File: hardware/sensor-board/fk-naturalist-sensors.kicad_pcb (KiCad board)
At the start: 2 copper layers, 20 x 32 mm, 18 parts, among them J1 Conn_01x07, M1 MOUNT_HOLE, M2 MOUNT_HOLE, M3 MOUNT_HOLE, M4 MOUNT_HOLE, U1 MPL3115A2, U2 SHT31, U3 SPH0645, U4 TSL2591

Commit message: Adding fiducials to the sensor board.
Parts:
- added M5: FIDUCIAL, Fiducials:Fiducial_0.75mm_Dia_1.5mm_Outer, F.Cu at (230.3, 129.8)
- added M6: FIDUCIAL, Fiducials:Fiducial_0.75mm_Dia_1.5mm_Outer, F.Cu at (237.9, 113.1)
- added M7: FIDUCIAL, Fiducials:Fiducial_0.75mm_Dia_1.5mm_Outer, F.Cu at (222.0, 109.9)
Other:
- board text added: "v0.9"
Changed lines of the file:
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@@
-(kicad_pcb (version 4) (host pcbnew 4.0.7-e2-6376~58~ubuntu16.04.1)
+(kicad_pcb (version 4) (host pcbnew 4.0.7)
   (general
     (links 39)
-    (no_connects 0)
+    (no_connects 14)
     (area 219.924999 99.924999 240.075001 132.075001)
     (thickness 1.6)
-    (drawings 4)
+    (drawings 5)
     (tracks 123)
     (zones 0)
-    (modules 18)
-    (nets 16)
+    (modules 21)
+    (nets 19)
   )
   (page A4)
@@
   (net 14 "Net-(U4-Pad2)")
   (net 15 "Net-(U4-Pad4)")
+  (net 16 "Net-(M5-Pad~)")
+  (net 17 "Net-(M6-Pad~)")
+  (net 18 "Net-(M7-Pad~)")
   (net_class Default "This is the default net class."
     (clearance 0.2)
@@
     (add_net GND)
     (add_net "Net-(C1-Pad1)")
+    (add_net "Net-(M5-Pad~)")
+    (add_net "Net-(M6-Pad~)")
+    (add_net "Net-(M7-Pad~)")
     (add_net "Net-(R1-Pad2)")
     (add_net "Net-(R2-Pad1)")
@@
     )
   )
+  (module Fiducials:Fiducial_0.75mm_Dia_1.5mm_Outer (layer F.Cu)
+    (at 230.251 129.794)
+    (descr "Circular Fiducial, 0.75mm bare copper top; 1.5mm keepout (Level B)")
+    (tags marker)
+    (attr virtual)
+    (fp_text reference M5 (at 0 -2) (layer F.SilkS) hide
+      (effects (font (size 1 1) (thickness 0.15)))
+    )
+    (fp_text value FIDUCIAL (at 0 2) (layer F.Fab) hide
+      (effects (font (size 1 1) (thickness 0.15)))
+    )
+    (fp_circle (center 0 0) (end 0.75 0) (layer F.Fab) (width 0.1))
+    (fp_text user %R (at 0 0) (layer F.Fab)
+      (effects (font (size 0.3 0.3) (thickness 0.05)))
+    )
+    (fp_circle (center 0 0) (end 1 0) (layer F.CrtYd) (width 0.05))
+    (pad ~ smd circle (at 0 0) (size 0.75 0.75) (layers F.Cu F.Mask)
+      (net 16 "Net-(M5-Pad~)") (solder_mask_margin 0.375) (clearance 0.375))
+  )
+  (module Fiducials:Fiducial_0.75mm_Dia_1.5mm_Outer (layer F.Cu)
+    (at 237.874 113.119001)
+    (descr "Circular Fiducial, 0.75mm bare copper top; 1.5mm keepout (Level B)")
+    (tags marker)
+    (attr virtual)
+    (fp_text reference M6 (at 0 -2) (layer F.SilkS) hide
+      (effects (font (size 1 1) (thickness 0.15)))
+    )
+    (fp_text value FIDUCIAL (at 0 2) (layer F.Fab) hide
+      (effects (font (size 1 1) (thickness 0.15)))
+    )
+    (fp_circle (center 0 0) (end 0.75 0) (layer F.Fab) (width 0.1))
+    (fp_text user %R (at 0 0) (layer F.Fab)
+      (effects (font (size 0.3 0.3) (thickness 0.05)))
+    )
+    (fp_circle (center 0 0) (end 1 0) (layer F.CrtYd) (width 0.05))
+    (pad ~ smd circle (at 0 0) (size 0.75 0.75) (layers F.Cu F.Mask)
+      (net 17 "Net-(M6-Pad~)") (solder_mask_margin 0.375) (clearance 0.375))
+  )
+  (module Fiducials:Fiducial_0.75mm_Dia_1.5mm_Outer (layer F.Cu)
+    (at 221.996 109.855)
+    (descr "Circular Fiducial, 0.75mm bare copper top; 1.5mm keepout (Level B)")
+    (tags marker)
+    (attr virtual)
+    (fp_text reference M7 (at 0 -2) (layer F.SilkS) hide
+      (effects (font (size 1 1) (thickness 0.15)))
+    )
+    (fp_text value FIDUCIAL (at 0 2) (layer F.Fab) hide
+      (effects (font (size 1 1) (thickness 0.15)))
+    )
+    (fp_circle (center 0 0) (end 0.75 0) (layer F.Fab) (width 0.1))
+    (fp_text user %R (at 0 0) (layer F.Fab)
+      (effects (font (size 0.3 0.3) (thickness 0.05)))
+    )
+    (fp_circle (center 0 0) (end 1 0) (layer F.CrtYd) (width 0.05))
+    (pad ~ smd circle (at 0 0) (size 0.75 0.75) (layers F.Cu F.Mask)
+      (net 18 "Net-(M7-Pad~)") (solder_mask_margin 0.375) (clearance 0.375))
+  )
+  (gr_text v0.9 (at 228.219 101.473 180) (layer F.SilkS)
+    (effects (font (size 1.5 1.5) (thickness 0.3)))
+  )
   (gr_line (start 240 100) (end 220 100) (layer Edge.Cuts) (width 0.15))

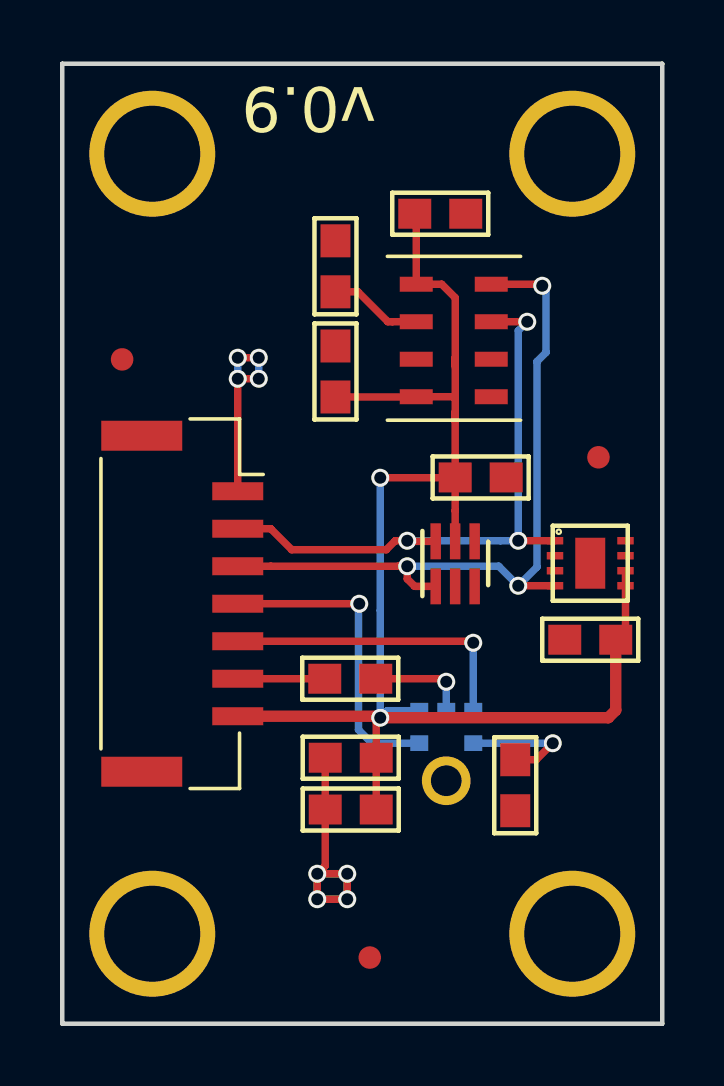
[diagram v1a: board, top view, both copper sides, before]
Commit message: Using new SPH0645 footprint.
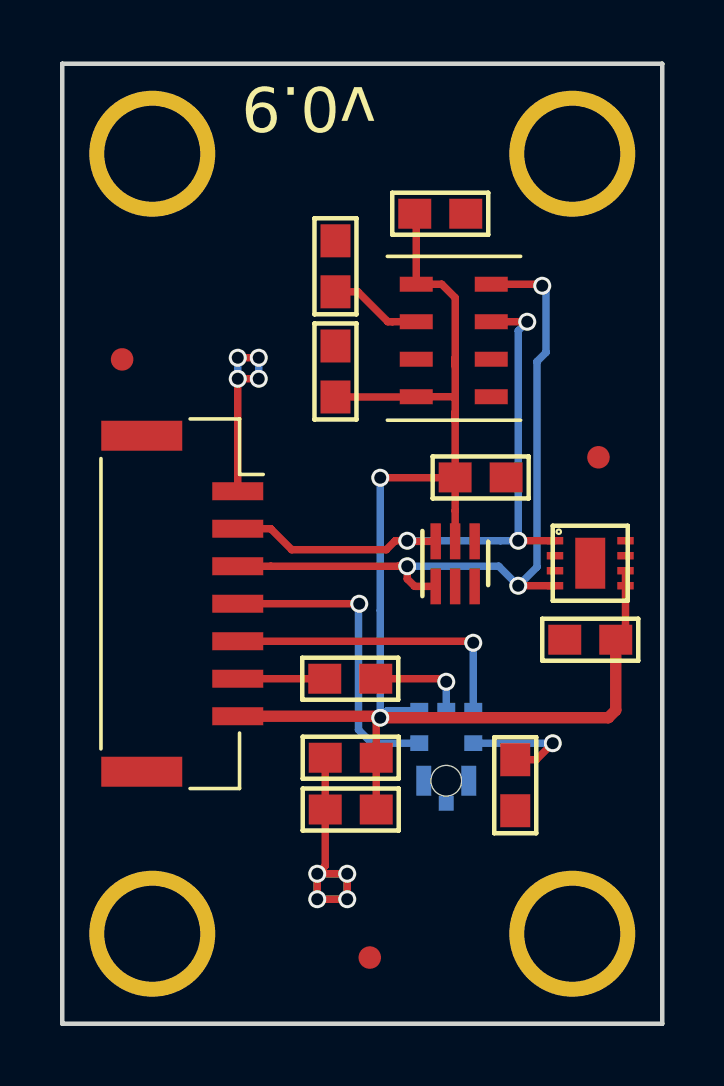
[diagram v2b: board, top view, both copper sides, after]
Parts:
- U3: footprint conservify:SPH0645LM4H-B -> SPH0645LM4H-B-SMD-GND
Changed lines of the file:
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@@
 (kicad_pcb (version 4) (host pcbnew 4.0.7)
   (general
-    (links 39)
-    (no_connects 14)
-    (area 219.924999 99.924999 240.075001 132.075001)
+    (links 41)
+    (no_connects 3)
+    (area 217.990476 98.85 242.009524 133.25)
     (thickness 1.6)
     (drawings 5)
@@
     (37 F.SilkS user)
     (38 B.Mask user)
-    (39 F.Mask user)
+    (39 F.Mask user hide)
     (40 Dwgs.User user)
     (41 Cmts.User user)
@@
     (add_net "Net-(U4-Pad4)")
   )
+  (module SPH0645LM4H-B-SMD-GND (layer B.Cu)
+    (at 232.8 123.9 180)
+    (fp_text reference U3 (at 0 3.302 180) (layer B.SilkS) hide
+      (effects (font (size 1 1) (thickness 0.15)) (justify mirror))
+    )
+    (fp_text value SPH0645 (at 0 -1.8 180) (layer B.Fab) hide
+      (effects (font (size 1 1) (thickness 0.15)) (justify mirror))
+    )
+    (fp_circle (center 0 0) (end 0.5 0) (layer Dwgs.User) (width 0.01))
+    (fp_circle (center 0 0) (end 0.8 0.05) (layer Dwgs.User) (width 0.01))
+    (fp_line (start -1.4 -1) (end 1.4 -1) (layer B.SilkS) (width 0.1))
+    (fp_line (start 1.4 -1) (end 1.4 2.7) (layer B.SilkS) (width 0.1))
+    (fp_line (start 1.4 2.7) (end -1.4 2.7) (layer B.SilkS) (width 0.1))
+    (fp_line (start -1.4 2.7) (end -1.4 -1) (layer B.SilkS) (width 0.1))
+    (pad 4 smd rect (at 0.9 1.252 180) (size 0.6 0.522) (layers B.Cu B.Paste B.Mask)
+      (net 12 /I2S_BCLK))
+    (pad 5 smd rect (at 0.9 2.335 180) (size 0.6 0.522) (layers B.Cu B.Paste B.Mask)
+      (net 3 3V3))
+    (pad 2 smd rect (at -0.9 1.252 180) (size 0.6 0.522) (layers B.Cu B.Paste B.Mask)
+      (net 4 "Net-(R1-Pad2)"))
+    (pad 1 smd rect (at -0.9 2.335 180) (size 0.6 0.522) (layers B.Cu B.Paste B.Mask)
+      (net 13 /I2S_WS))
+    (pad "" np_thru_hole circle (at 0 0 180) (size 1.024 1.024) (drill 1.024) (layers *.Cu *.Mask))
+    (pad 6 smd rect (at 0 2.335 180) (size 0.6 0.522) (layers B.Cu B.Paste B.Mask)
+      (net 5 "Net-(R2-Pad1)"))
+    (pad 3 smd rect (at 0.75 0 180) (size 0.5 1) (layers B.Cu B.Paste B.Mask)
+      (net 2 GND))
+    (pad 3 smd rect (at -0.75 0 180) (size 0.5 1) (layers B.Cu B.Paste B.Mask)
+      (net 2 GND))
+    (pad 3 smd rect (at 0 -0.75 180) (size 0.5 0.5) (layers B.Cu B.Paste B.Mask)
+      (net 2 GND))
+  )
   (module RocketScreamKicadLibrary:CAP-0603 (layer F.Cu)
     (at 229.1072 106.7528 90)
@@
     (pad PAD smd rect (at 0 0) (size 1 1.7) (layers F.Cu F.Paste F.Mask)
       (net 2 GND) (solder_paste_margin -0.05))
-  )
-  (module conservify:SPH0645LM4H-B (layer B.Cu)
-    (at 232.8 123.9 180)
-    (fp_text reference U3 (at 0 3.302 180) (layer B.SilkS) hide
-      (effects (font (size 1 1) (thickness 0.15)) (justify mirror))
-    )
-    (fp_text value SPH0645 (at 0 -1.8 180) (layer B.Fab) hide
-      (effects (font (size 1 1) (thickness 0.15)) (justify mirror))
-    )
-    (fp_line (start -1.4 -1) (end 1.4 -1) (layer B.SilkS) (width 0.1))
-    (fp_line (start 1.4 -1) (end 1.4 2.7) (layer B.SilkS) (width 0.1))
-    (fp_line (start 1.4 2.7) (end -1.4 2.7) (layer B.SilkS) (width 0.1))
-    (fp_line (start -1.4 2.7) (end -1.4 -1) (layer B.SilkS) (width 0.1))
-    (pad 4 smd rect (at 0.9 1.252 180) (size 0.6 0.522) (layers B.Cu B.Paste B.Mask)
-      (net 12 /I2S_BCLK))
-    (pad 5 smd rect (at 0.9 2.335 180) (size 0.6 0.522) (layers B.Cu B.Paste B.Mask)
-      (net 3 3V3))
-    (pad 2 smd rect (at -0.9 1.252 180) (size 0.6 0.522) (layers B.Cu B.Paste B.Mask)
-      (net 4 "Net-(R1-Pad2)"))
-    (pad 1 smd rect (at -0.9 2.335 180) (size 0.6 0.522) (layers B.Cu B.Paste B.Mask)
-      (net 13 /I2S_WS))
-    (pad 3 thru_hole circle (at 0 0 180) (size 1.624 1.624) (drill 1.024) (layers *.Cu *.Mask B.Paste B.SilkS)
-      (net 2 GND))
-    (pad 6 smd rect (at 0 2.335 180) (size 0.6 0.522) (layers B.Cu B.Paste B.Mask)
-      (net 5 "Net-(R2-Pad1)"))
   )
   (module conservify:TSL2591 (layer F.Cu)
@@
     (connect_pads (clearance 0.2032))
     (min_thickness 0.2032)
-    (fill (arc_segments 32) (thermal_gap 0.254) (thermal_bridge_width 0.254))
+    (fill yes (arc_segments 32) (thermal_gap 0.254) (thermal_bridge_width 0.254))
     (polygon
       (pts
@@
     (connect_pads (clearance 0.2032))
     (min_thickness 0.2032)
-    (fill (arc_segments 32) (thermal_gap 0.254) (thermal_bridge_width 0.254))
+    (fill yes (arc_segments 32) (thermal_gap 0.254) (thermal_bridge_width 0.254))
     (polygon
       (pts

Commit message: Plot sensor board.
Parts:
- added G***: LOGO, conservify:fk_negative_2500, F.Cu at (238.0, 109.2)
- added G***: LOGO, conservify:conservify_text_negative_4000, B.Cu at (223.6, 116.1)
- moved M6 1.05 mm to (237.9, 114.2)

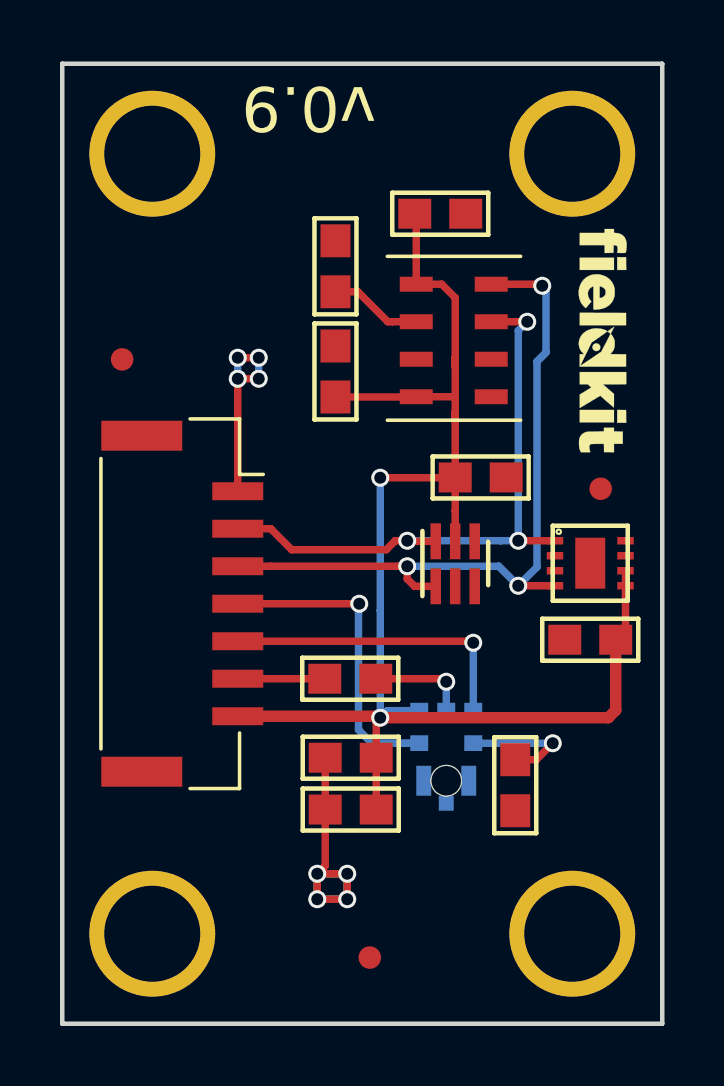
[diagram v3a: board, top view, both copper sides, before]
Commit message: Adding fiducials to the bottom.
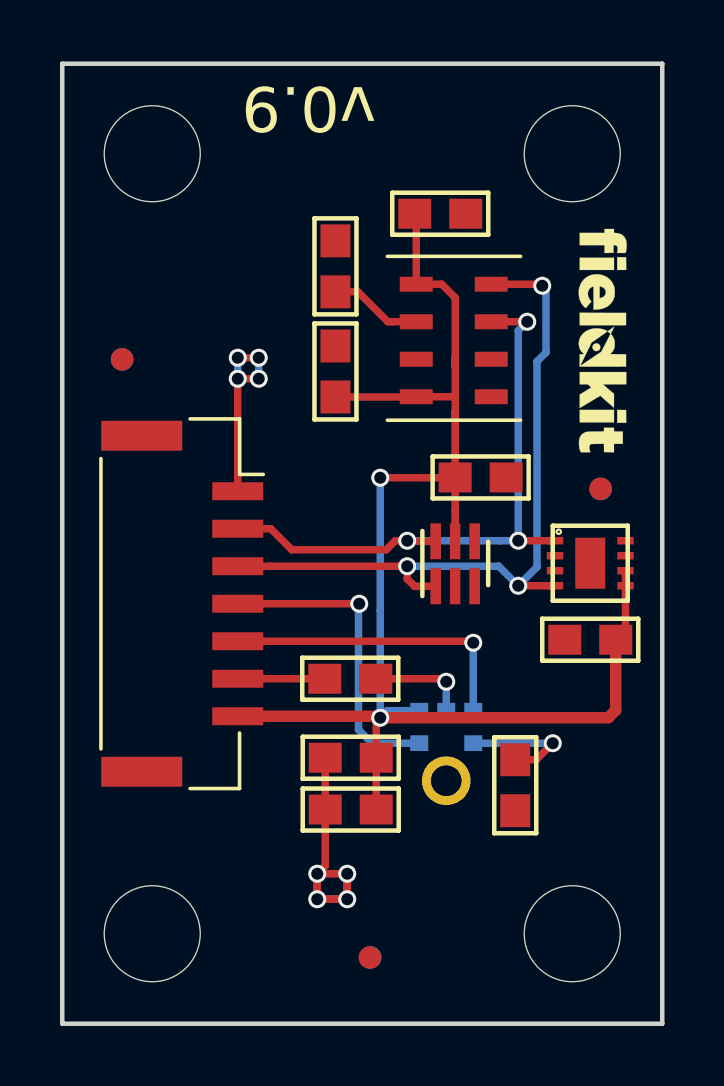
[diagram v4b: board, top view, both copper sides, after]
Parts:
- added M10: FIDUCIAL, Fiducials:Fiducial_0.75mm_Dia_1.5mm_Outer, B.Cu at (237.9, 114.2)
- added M8: FIDUCIAL, Fiducials:Fiducial_0.75mm_Dia_1.5mm_Outer, B.Cu at (230.3, 129.8)
- added M9: FIDUCIAL, Fiducials:Fiducial_0.75mm_Dia_1.5mm_Outer, B.Cu at (222.0, 109.9)
- M1, M2, M3, M4: footprint RocketScreamKicadLibrary:HOLE_PTH_3.2MM -> conservify:HOLE_NPTH_3.2MM
- U3: footprint SPH0645LM4H-B-SMD-GND -> conservify:SPH0645LM4H-B
